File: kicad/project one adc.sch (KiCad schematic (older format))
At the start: 0 parts

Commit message: ..more work
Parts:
- added C? (x14): 0.33uF, ~, symbol CSMALL
- added C? (x3): 0.1uF, ~, symbol CSMALL
- added C? (x5): 10uF, ~, symbol CPSMALL
- added J? (x6): SJ-43416-SMT-GR, ~, symbol JACK_6P
- added U?: PCM1851A, symbol PCM1851A
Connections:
- net labels added: +3.3V, +5VA, GND, IISC, IISC_IMCK, IISC_ISCK, IISC_ISDI, IISC_IWS, OVER, TWIMS0, TWIMS0_TWCK, TWIMS0_TWD, VinL 1, VinL 2, VinL 3, VinL 4, VinL 5, VinL 6, VinR 1, VinR 2, VinR 3, VinR 4, VinR 5, VinR 6, ~RESET
- wire segments 0 -> 126
- no-connect marks 0 -> 2
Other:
- note added: "LINE IN 1"
- note added: "LINE IN 2"
- note added: "LINE IN 3"
- note added: "LINE IN 4"
- note added: "LINE IN 5"
- note added: "LINE IN 6"

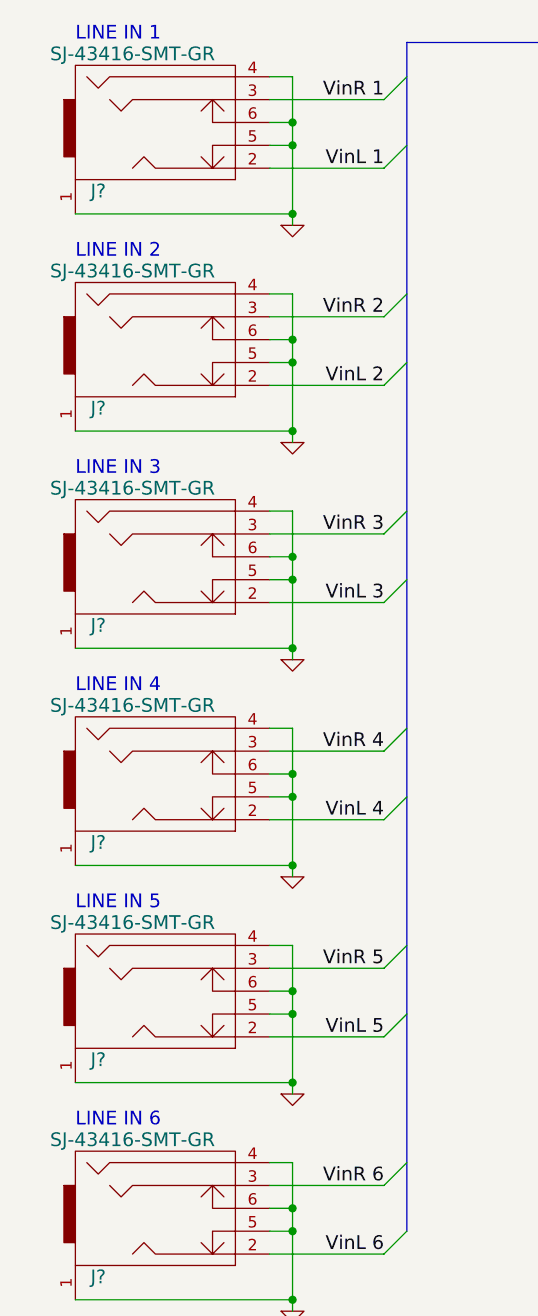
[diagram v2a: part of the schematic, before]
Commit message: Work on amplifier sheeet
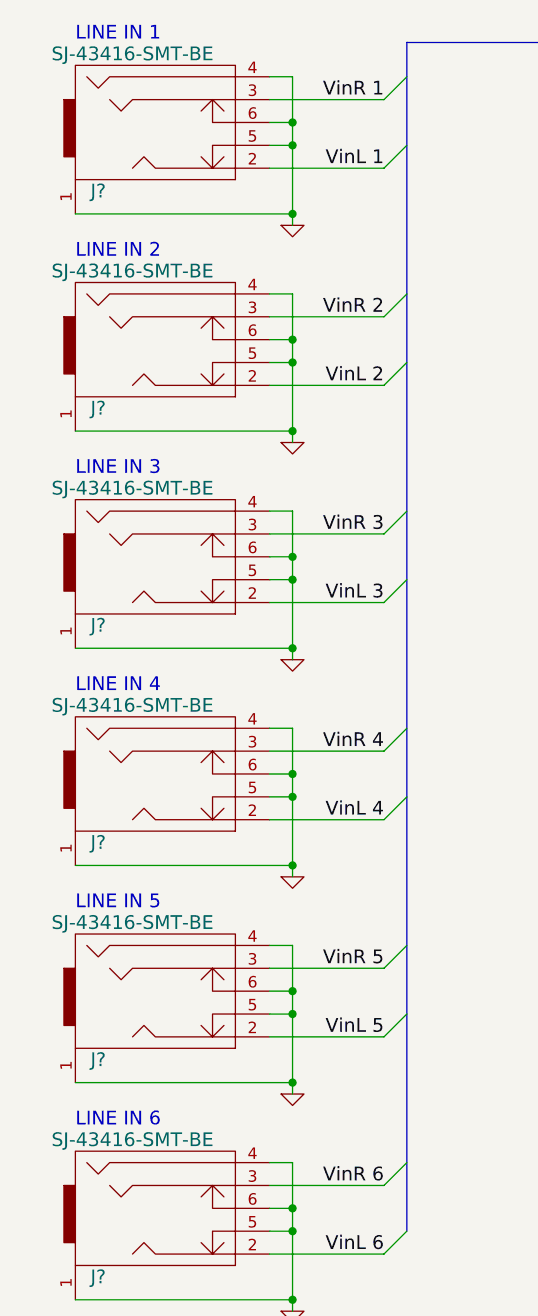
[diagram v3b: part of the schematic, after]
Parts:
- removed J? (x5): SJ-43416-SMT-GR, ~, symbol JACK_6P
- added J? (x5): SJ-43416-SMT-BE, ~, symbol JACK_6P
- J?: value SJ-43416-SMT-GR -> SJ-43416-SMT-BE
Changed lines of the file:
@@
 P 1450 1250
 F 0 "J?" H 1150 1000 60  0000 C CNN
-F 1 "SJ-43416-SMT-GR" H 1300 1600 60  0000 C CNN
+F 1 "SJ-43416-SMT-BE" H 1300 1600 60  0000 C CNN
 F 2 "~" H 1450 1250 60  0000 C CNN
 F 3 "~" H 1450 1250 60  0000 C CNN
@@
 LINE IN 1
 $Comp
-L JACK_6P J?
-U 1 1 5367405B
-P 1450 2200
-F 0 "J?" H 1150 1950 60  0000 C CNN
-F 1 "SJ-43416-SMT-GR" H 1300 2550 60  0000 C CNN
-F 2 "~" H 1450 2200 60  0000 C CNN
-F 3 "~" H 1450 2200 60  0000 C CNN
-	1    1450 2200
-	1    0    0    -1
-$EndComp
-$Comp
 L GND #PWR?
 U 1 1 53674061
@@
 $EndComp
 $Comp
-L JACK_6P J?
-U 1 1 53674070
-P 1450 3150
-F 0 "J?" H 1150 2900 60  0000 C CNN
-F 1 "SJ-43416-SMT-GR" H 1300 3500 60  0000 C CNN
-F 2 "~" H 1450 3150 60  0000 C CNN
-F 3 "~" H 1450 3150 60  0000 C CNN
-	1    1450 3150
-	1    0    0    -1
-$EndComp
-$Comp
 L GND #PWR?
 U 1 1 53674076
@@
 $EndComp
 $Comp
-L JACK_6P J?
-U 1 1 53674085
-P 1450 4100
-F 0 "J?" H 1150 3850 60  0000 C CNN
-F 1 "SJ-43416-SMT-GR" H 1300 4450 60  0000 C CNN
-F 2 "~" H 1450 4100 60  0000 C CNN
-F 3 "~" H 1450 4100 60  0000 C CNN
-	1    1450 4100
-	1    0    0    -1
-$EndComp
-$Comp
 L GND #PWR?
 U 1 1 5367408B
@@
 $EndComp
 $Comp
-L JACK_6P J?
-U 1 1 5367409A
-P 1450 5050
-F 0 "J?" H 1150 4800 60  0000 C CNN
-F 1 "SJ-43416-SMT-GR" H 1300 5400 60  0000 C CNN
-F 2 "~" H 1450 5050 60  0000 C CNN
-F 3 "~" H 1450 5050 60  0000 C CNN
-	1    1450 5050
-	1    0    0    -1
-$EndComp
-$Comp
 L GND #PWR?
 U 1 1 536740A0
@@
 F 3 "" H 2000 5450 60  0000 C CNN
 	1    2000 5450
-	1    0    0    -1
-$EndComp
-$Comp
-L JACK_6P J?
-U 1 1 536740AF
-P 1450 6000
-F 0 "J?" H 1150 5750 60  0000 C CNN
-F 1 "SJ-43416-SMT-GR" H 1300 6350 60  0000 C CNN
-F 2 "~" H 1450 6000 60  0000 C CNN
-F 3 "~" H 1450 6000 60  0000 C CNN
-	1    1450 6000
 	1    0    0    -1
 $EndComp
@@
 Wire Bus Line
 	2500 850  2500 6050
+$Comp
+L JACK_6P J?
+U 1 1 536800A2
+P 1450 2200
+F 0 "J?" H 1150 1950 60  0000 C CNN
+F 1 "SJ-43416-SMT-BE" H 1300 2550 60  0000 C CNN
+F 2 "~" H 1450 2200 60  0000 C CNN
+F 3 "~" H 1450 2200 60  0000 C CNN
+	1    1450 2200
+	1    0    0    -1
+$EndComp
+$Comp
+L JACK_6P J?
+U 1 1 536800A8
+P 1450 3150
+F 0 "J?" H 1150 2900 60  0000 C CNN
+F 1 "SJ-43416-SMT-BE" H 1300 3500 60  0000 C CNN
+F 2 "~" H 1450 3150 60  0000 C CNN
+F 3 "~" H 1450 3150 60  0000 C CNN
+	1    1450 3150
+	1    0    0    -1
+$EndComp
+$Comp
+L JACK_6P J?
+U 1 1 536800AE
+P 1450 4100
+F 0 "J?" H 1150 3850 60  0000 C CNN
+F 1 "SJ-43416-SMT-BE" H 1300 4450 60  0000 C CNN
+F 2 "~" H 1450 4100 60  0000 C CNN
+F 3 "~" H 1450 4100 60  0000 C CNN
+	1    1450 4100
+	1    0    0    -1
+$EndComp
+$Comp
+L JACK_6P J?
+U 1 1 536800B4
+P 1450 5050
+F 0 "J?" H 1150 4800 60  0000 C CNN
+F 1 "SJ-43416-SMT-BE" H 1300 5400 60  0000 C CNN
+F 2 "~" H 1450 5050 60  0000 C CNN
+F 3 "~" H 1450 5050 60  0000 C CNN
+	1    1450 5050
+	1    0    0    -1
+$EndComp
+$Comp
+L JACK_6P J?
+U 1 1 536800BA
+P 1450 6000
+F 0 "J?" H 1150 5750 60  0000 C CNN
+F 1 "SJ-43416-SMT-BE" H 1300 6350 60  0000 C CNN
+F 2 "~" H 1450 6000 60  0000 C CNN
+F 3 "~" H 1450 6000 60  0000 C CNN
+	1    1450 6000
+	1    0    0    -1
+$EndComp
 $EndSCHEMATC

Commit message: Forgot to add annotation
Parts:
- gave numbers to parts that had none: 29
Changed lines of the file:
@@
 $EndDescr
 $Comp
-L JACK_6P J?
+L JACK_6P J401
 U 1 1 53674004
 P 1450 1250
-F 0 "J?" H 1150 1000 60  0000 C CNN
+F 0 "J401" H 1150 1000 60  0000 C CNN
 F 1 "SJ-43416-SMT-BE" H 1300 1600 60  0000 C CNN
 F 2 "~" H 1450 1250 60  0000 C CNN
@@
 $EndComp
 $Comp
-L GND #PWR?
+L GND #PWR401
 U 1 1 5367402B
 P 2000 1650
-F 0 "#PWR?" H 2000 1650 30  0001 C CNN
+F 0 "#PWR401" H 2000 1650 30  0001 C CNN
 F 1 "GND" H 2000 1580 30  0001 C CNN
 F 2 "" H 2000 1650 60  0000 C CNN
@@
 LINE IN 1
 $Comp
-L GND #PWR?
+L GND #PWR402
 U 1 1 53674061
 P 2000 2600
-F 0 "#PWR?" H 2000 2600 30  0001 C CNN
+F 0 "#PWR402" H 2000 2600 30  0001 C CNN
 F 1 "GND" H 2000 2530 30  0001 C CNN
 F 2 "" H 2000 2600 60  0000 C CNN
@@
 $EndComp
 $Comp
-L GND #PWR?
+L GND #PWR403
 U 1 1 53674076
 P 2000 3550
-F 0 "#PWR?" H 2000 3550 30  0001 C CNN
+F 0 "#PWR403" H 2000 3550 30  0001 C CNN
 F 1 "GND" H 2000 3480 30  0001 C CNN
 F 2 "" H 2000 3550 60  0000 C CNN
@@
 $EndComp
 $Comp
-L GND #PWR?
+L GND #PWR404
 U 1 1 5367408B
 P 2000 4500
-F 0 "#PWR?" H 2000 4500 30  0001 C CNN
+F 0 "#PWR404" H 2000 4500 30  0001 C CNN
 F 1 "GND" H 2000 4430 30  0001 C CNN
 F 2 "" H 2000 4500 60  0000 C CNN
@@
 $EndComp
 $Comp
-L GND #PWR?
+L GND #PWR405
 U 1 1 536740A0
 P 2000 5450
-F 0 "#PWR?" H 2000 5450 30  0001 C CNN
+F 0 "#PWR405" H 2000 5450 30  0001 C CNN
 F 1 "GND" H 2000 5380 30  0001 C CNN
 F 2 "" H 2000 5450 60  0000 C CNN
@@
 $EndComp
 $Comp
-L GND #PWR?
+L GND #PWR406
 U 1 1 536740B5
 P 2000 6400
-F 0 "#PWR?" H 2000 6400 30  0001 C CNN
+F 0 "#PWR406" H 2000 6400 30  0001 C CNN
 F 1 "GND" H 2000 6330 30  0001 C CNN
 F 2 "" H 2000 6400 60  0000 C CNN
@@
 VinR 6
 $Comp
-L PCM1851A U?
+L PCM1851A U401
 U 1 1 5366EF69
 P 6100 3300
-F 0 "U?" H 5450 4050 60  0000 C CNN
+F 0 "U401" H 5450 4050 60  0000 C CNN
 F 1 "PCM1851A" H 6100 3300 60  0000 C CNN
 F 2 "" H 5950 3300 60  0000 C CNN
@@
 $EndComp
 $Comp
-L CSMALL C?
+L CSMALL C409
 U 1 1 5366EFD1
 P 4950 3150
-F 0 "C?" H 4975 3200 30  0000 L CNN
+F 0 "C409" H 4975 3200 30  0000 L CNN
 F 1 "0.33uF" V 5000 2950 30  0000 L CNN
 F 2 "~" H 4950 3150 60  0000 C CNN
@@
 VinR 2
 $Comp
-L CSMALL C?
+L CSMALL C408
 U 1 1 5366F19F
 P 4950 2900
-F 0 "C?" H 4975 2950 30  0000 L CNN
+F 0 "C408" H 4975 2950 30  0000 L CNN
 F 1 "0.33uF" V 5000 2700 30  0000 L CNN
 F 2 "~" H 4950 2900 60  0000 C CNN
@@
 $EndComp
 $Comp
-L CSMALL C?
+L CSMALL C407
 U 1 1 5366F1A5
 P 4950 2650
-F 0 "C?" H 4975 2700 30  0000 L CNN
+F 0 "C407" H 4975 2700 30  0000 L CNN
 F 1 "0.33uF" V 5000 2450 30  0000 L CNN
 F 2 "~" H 4950 2650 60  0000 C CNN
@@
 $EndComp
 $Comp
-L CSMALL C?
+L CSMALL C410
 U 1 1 5366F1AB
 P 4950 3400
-F 0 "C?" H 4975 3450 30  0000 L CNN
+F 0 "C410" H 4975 3450 30  0000 L CNN
 F 1 "0.33uF" V 5000 3200 30  0000 L CNN
 F 2 "~" H 4950 3400 60  0000 C CNN
@@
 $EndComp
 $Comp
-L CSMALL C?
+L CSMALL C411
 U 1 1 5366F1B1
 P 4950 3650
-F 0 "C?" H 4975 3700 30  0000 L CNN
+F 0 "C411" H 4975 3700 30  0000 L CNN
 F 1 "0.33uF" V 5000 3450 30  0000 L CNN
 F 2 "~" H 4950 3650 60  0000 C CNN
@@
 $EndComp
 $Comp
-L CSMALL C?
+L CSMALL C412
 U 1 1 5366F1B7
 P 4950 3900
-F 0 "C?" H 4975 3950 30  0000 L CNN
+F 0 "C412" H 4975 3950 30  0000 L CNN
 F 1 "0.33uF" V 5000 3700 30  0000 L CNN
 F 2 "~" H 4950 3900 60  0000 C CNN
@@
 $EndComp
 $Comp
-L CSMALL C?
+L CSMALL C406
 U 1 1 5366F1BD
 P 4700 4000
-F 0 "C?" H 4725 4050 30  0000 L CNN
+F 0 "C406" H 4725 4050 30  0000 L CNN
 F 1 "0.33uF" V 4750 3800 30  0000 L CNN
 F 2 "~" H 4700 4000 60  0000 C CNN
@@
 $EndComp
 $Comp
-L CSMALL C?
+L CSMALL C405
 U 1 1 5366F1D5
 P 4700 3750
-F 0 "C?" H 4725 3800 30  0000 L CNN
+F 0 "C405" H 4725 3800 30  0000 L CNN
 F 1 "0.33uF" V 4750 3550 30  0000 L CNN
 F 2 "~" H 4700 3750 60  0000 C CNN
@@
 $EndComp
 $Comp
-L CSMALL C?
+L CSMALL C404
 U 1 1 5366F1DB
 P 4700 3500
-F 0 "C?" H 4725 3550 30  0000 L CNN
+F 0 "C404" H 4725 3550 30  0000 L CNN
 F 1 "0.33uF" V 4750 3300 30  0000 L CNN
 F 2 "~" H 4700 3500 60  0000 C CNN
@@
 $EndComp
 $Comp
-L CSMALL C?
+L CSMALL C403
 U 1 1 5366F1E1
 P 4700 3250
-F 0 "C?" H 4725 3300 30  0000 L CNN
+F 0 "C403" H 4725 3300 30  0000 L CNN
 F 1 "0.33uF" V 4750 3050 30  0000 L CNN
 F 2 "~" H 4700 3250 60  0000 C CNN
@@
 $EndComp
 $Comp
-L CSMALL C?
+L CSMALL C402
 U 1 1 5366F1E7
 P 4700 3000
-F 0 "C?" H 4725 3050 30  0000 L CNN
+F 0 "C402" H 4725 3050 30  0000 L CNN
 F 1 "0.33uF" V 4750 2800 30  0000 L CNN
 F 2 "~" H 4700 3000 60  0000 C CNN
@@
 $EndComp
 $Comp
-L CSMALL C?
+L CSMALL C401
 U 1 1 5366F1ED
 P 4700 2750
-F 0 "C?" H 4725 2800 30  0000 L CNN
+F 0 "C401" H 4725 2800 30  0000 L CNN
 F 1 "0.33uF" V 4750 2550 30  0000 L CNN
 F 2 "~" H 4700 2750 60  0000 C CNN
@@
 NoConn ~ 7100 4000
 $Comp
-L GND #PWR?
+L GND #PWR410
 U 1 1 53670AE5
 P 6250 4850
-F 0 "#PWR?" H 6250 4850 30  0001 C CNN
+F 0 "#PWR410" H 6250 4850 30  0001 C CNN
 F 1 "GND" H 6250 4780 30  0001 C CNN
 F 2 "" H 6250 4850 60  0000 C CNN
@@
 $EndComp
 $Comp
-L CSMALL C?
+L CSMALL C416
 U 1 1 53670D36
 P 6050 5150
-F 0 "C?" H 6075 5200 30  0000 L CNN
+F 0 "C416" H 6075 5200 30  0000 L CNN
 F 1 "0.1uF" V 6100 5000 30  0000 L CNN
 F 2 "~" H 6050 5150 60  0000 C CNN
@@
 $EndComp
 $Comp
-L CPSMALL C?
+L CPSMALL C415
 U 1 1 53670D54
 P 5900 5150
-F 0 "C?" H 5925 5200 30  0000 L CNN
+F 0 "C415" H 5925 5200 30  0000 L CNN
 F 1 "10uF" V 5950 5000 30  0000 L CNN
 F 2 "~" H 5900 5150 60  0000 C CNN
@@
 $EndComp
 $Comp
-L GND #PWR?
+L GND #PWR408
 U 1 1 53670F5E
 P 5950 6100
-F 0 "#PWR?" H 5950 6100 30  0001 C CNN
+F 0 "#PWR408" H 5950 6100 30  0001 C CNN
 F 1 "GND" H 5950 6030 30  0001 C CNN
 F 2 "" H 5950 6100 60  0000 C CNN
@@
 $EndComp
 $Comp
-L CSMALL C?
+L CSMALL C414
 U 1 1 53670FCF
 P 5850 5450
-F 0 "C?" H 5875 5500 30  0000 L CNN
+F 0 "C414" H 5875 5500 30  0000 L CNN
 F 1 "0.1uF" V 5900 5300 30  0000 L CNN
 F 2 "~" H 5850 5450 60  0000 C CNN
@@
 $EndComp
 $Comp
-L CPSMALL C?
+L CPSMALL C413
 U 1 1 53670FD5
 P 5700 5450
-F 0 "C?" H 5725 5500 30  0000 L CNN
+F 0 "C413" H 5725 5500 30  0000 L CNN
 F 1 "10uF" V 5750 5300 30  0000 L CNN
 F 2 "~" H 5700 5450 60  0000 C CNN
@@
 $EndComp
 $Comp
-L CSMALL C?
+L CSMALL C418
 U 1 1 53670FE5
 P 6200 5550
-F 0 "C?" H 6225 5600 30  0000 L CNN
+F 0 "C418" H 6225 5600 30  0000 L CNN
 F 1 "0.1uF" V 6250 5400 30  0000 L CNN
 F 2 "~" H 6200 5550 60  0000 C CNN
@@
 $EndComp
 $Comp
-L CPSMALL C?
+L CPSMALL C417
 U 1 1 53670FEB
 P 6050 5550
-F 0 "C?" H 6075 5600 30  0000 L CNN
+F 0 "C417" H 6075 5600 30  0000 L CNN
 F 1 "10uF" V 6100 5400 30  0000 L CNN
 F 2 "~" H 6050 5550 60  0000 C CNN
@@
 $EndComp
 $Comp
-L +5VA #PWR?
+L +5VA #PWR407
 U 1 1 53671535
 P 5800 1700
-F 0 "#PWR?" H 5800 1830 20  0001 C CNN
+F 0 "#PWR407" H 5800 1830 20  0001 C CNN
 F 1 "+5VA" H 5800 1800 30  0000 C CNN
 F 2 "" H 5800 1700 60  0000 C CNN
@@
 $EndComp
 $Comp
-L +3.3V #PWR?
+L +3.3V #PWR409
 U 1 1 536715F1
 P 6100 1700
-F 0 "#PWR?" H 6100 1660 30  0001 C CNN
+F 0 "#PWR409" H 6100 1660 30  0001 C CNN
 F 1 "+3.3V" H 6100 1810 30  0000 C CNN
 F 2 "" H 6100 1700 60  0000 C CNN
@@
 $EndComp
 $Comp
-L CPSMALL C?
+L CPSMALL C419
 U 1 1 536716C1
 P 6400 1750
-F 0 "C?" H 6425 1800 30  0000 L CNN
+F 0 "C419" H 6425 1800 30  0000 L CNN
 F 1 "10uF" V 6450 1600 30  0000 L CNN
 F 2 "~" H 6400 1750 60  0000 C CNN
@@
 $EndComp
 $Comp
-L CSMALL C?
+L CSMALL C420
 U 1 1 536716D1
 P 6400 1900
-F 0 "C?" H 6425 1950 30  0000 L CNN
+F 0 "C420" H 6425 1950 30  0000 L CNN
 F 1 "0.33uF" V 6450 1700 30  0000 L CNN
 F 2 "~" H 6400 1900 60  0000 C CNN
@@
 $EndComp
 $Comp
-L CPSMALL C?
+L CPSMALL C421
 U 1 1 536716D7
 P 6400 2050
-F 0 "C?" H 6425 2100 30  0000 L CNN
+F 0 "C421" H 6425 2100 30  0000 L CNN
 F 1 "10uF" V 6450 1900 30  0000 L CNN
 F 2 "~" H 6400 2050 60  0000 C CNN
@@
 $EndComp
 $Comp
-L CSMALL C?
+L CSMALL C422
 U 1 1 536716DD
 P 6400 2200
-F 0 "C?" H 6425 2250 30  0000 L CNN
+F 0 "C422" H 6425 2250 30  0000 L CNN
 F 1 "0.33uF" V 6450 2000 30  0000 L CNN
 F 2 "~" H 6400 2200 60  0000 C CNN
@@
 $EndComp
 $Comp
-L GND #PWR?
+L GND #PWR411
 U 1 1 5367191E
 P 6650 2300
-F 0 "#PWR?" H 6650 2300 30  0001 C CNN
+F 0 "#PWR411" H 6650 2300 30  0001 C CNN
 F 1 "GND" H 6650 2230 30  0001 C CNN
 F 2 "" H 6650 2300 60  0000 C CNN
@@
 	2500 850  2500 6050
 $Comp
-L JACK_6P J?
+L JACK_6P J402
 U 1 1 536800A2
 P 1450 2200
-F 0 "J?" H 1150 1950 60  0000 C CNN
+F 0 "J402" H 1150 1950 60  0000 C CNN
 F 1 "SJ-43416-SMT-BE" H 1300 2550 60  0000 C CNN
 F 2 "~" H 1450 2200 60  0000 C CNN
@@
 $EndComp
 $Comp
-L JACK_6P J?
+L JACK_6P J403
 U 1 1 536800A8
 P 1450 3150
-F 0 "J?" H 1150 2900 60  0000 C CNN
+F 0 "J403" H 1150 2900 60  0000 C CNN
 F 1 "SJ-43416-SMT-BE" H 1300 3500 60  0000 C CNN
 F 2 "~" H 1450 3150 60  0000 C CNN
@@
 $EndComp
 $Comp
-L JACK_6P J?
+L JACK_6P J404
 U 1 1 536800AE
 P 1450 4100
-F 0 "J?" H 1150 3850 60  0000 C CNN
+F 0 "J404" H 1150 3850 60  0000 C CNN
 F 1 "SJ-43416-SMT-BE" H 1300 4450 60  0000 C CNN
 F 2 "~" H 1450 4100 60  0000 C CNN
@@
 $EndComp
 $Comp
-L JACK_6P J?
+L JACK_6P J405
 U 1 1 536800B4
 P 1450 5050
-F 0 "J?" H 1150 4800 60  0000 C CNN
+F 0 "J405" H 1150 4800 60  0000 C CNN
 F 1 "SJ-43416-SMT-BE" H 1300 5400 60  0000 C CNN
 F 2 "~" H 1450 5050 60  0000 C CNN
@@
 $EndComp
 $Comp
-L JACK_6P J?
+L JACK_6P J406
 U 1 1 536800BA
 P 1450 6000
-F 0 "J?" H 1150 5750 60  0000 C CNN
+F 0 "J406" H 1150 5750 60  0000 C CNN
 F 1 "SJ-43416-SMT-BE" H 1300 6350 60  0000 C CNN
 F 2 "~" H 1450 6000 60  0000 C CNN

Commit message: Work on tone control
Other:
- note added: "ESD protection needed"
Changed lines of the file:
@@
 Sheet 3 6
 Title "Project One"
-Date "9 may 2014"
+Date "27 may 2014"
 Rev "0.0.0"
 Comp "Ali Kocaturk"
@@
 	1    0    0    -1
 $EndComp
+Text Notes 2600 750  0    60   ~ 0
+ESD protection needed
 $EndSCHEMATC
